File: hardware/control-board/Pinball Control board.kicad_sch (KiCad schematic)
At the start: 108 parts, among them J1 Connector C, J3 B4B-XH-A, J4 Conn_01x10_Pin, J5 Conn_01x10_Pin, Q1 BSS138, Q10 BSS84, Q11 BSS138, Q12 BSS84, Q13 BSS138, Q14 BSS84, Q15 BSS138, Q16 IRFR5410, Q17 IRFR5410, Q18 IRFR5410, Q19 IRFR5410, Q2 BSS138, Q20 IRFR5410, Q3 BSS138, Q4 BSS138, Q5 BSS138, Q6 BSS84, Q7 BSS138, Q8 BSS84, Q9 BSS138, SW1 test switch, SW2 test switch

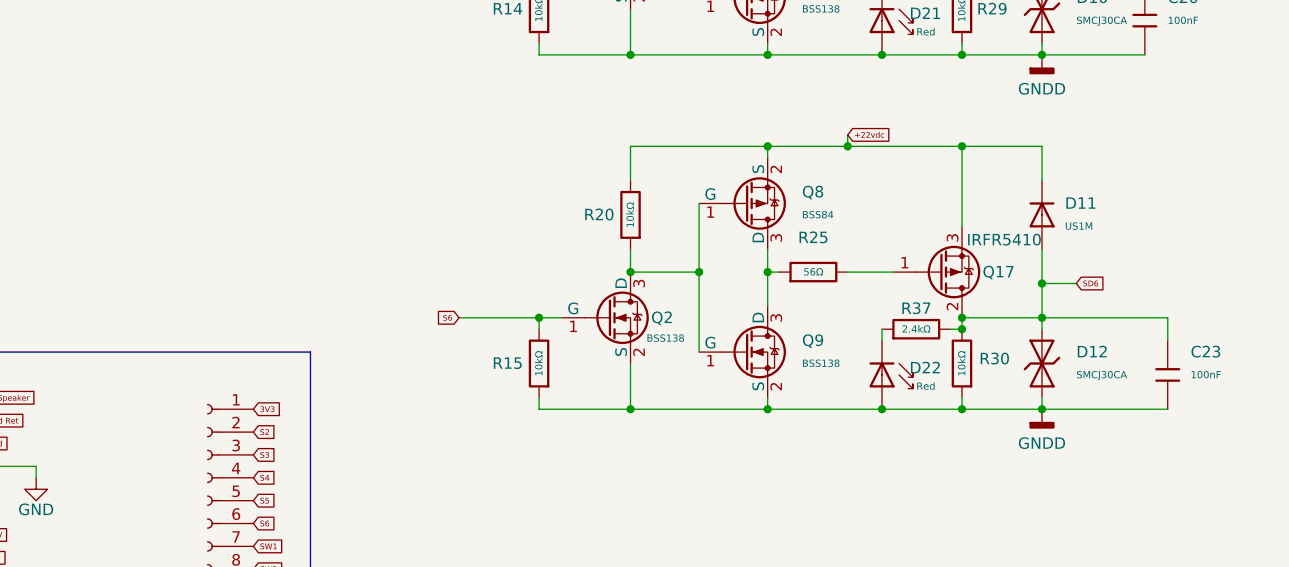
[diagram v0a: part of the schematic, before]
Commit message: Add KiCad note for single-channel solenoid respin
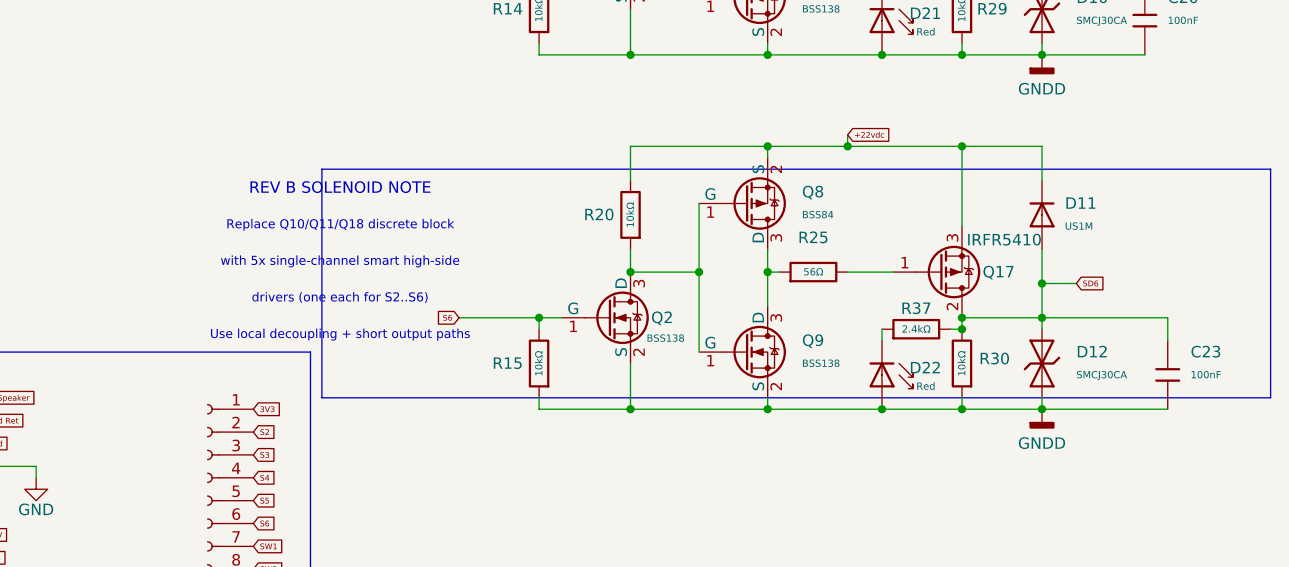
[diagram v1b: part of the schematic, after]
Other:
- note added: "REV B SOLENOID NOTE"
- note added: "Replace Q10/Q11/Q18 discrete block"
- note added: "Use local decoupling + short output paths"
- note added: "drivers (one each for S2..S6)"
- note added: "with 5x single-channel smart high-side"
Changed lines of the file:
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@@
+		)
+	)
+	(rectangle
+		(start 208.28 205.74)
+		(end 313.69 231.14)
+		(stroke
+			(width 0)
+			(type default)
+		)
+		(fill
+			(type none)
+		)
+	)
+	(text "REV B SOLENOID NOTE"
+		(exclude_from_sim no)
+		(at 210.312 208.026 0)
+		(effects
+			(font
+				(size 1.27 1.27)
+			)
+		)
+	)
+	(text "Replace Q10/Q11/Q18 discrete block"
+		(exclude_from_sim no)
+		(at 210.312 212.09 0)
+		(effects
+			(font
+				(size 1 1)
+			)
+		)
+	)
+	(text "with 5x single-channel smart high-side"
+		(exclude_from_sim no)
+		(at 210.312 216.154 0)
+		(effects
+			(font
+				(size 1 1)
+			)
+		)
+	)
+	(text "drivers (one each for S2..S6)"
+		(exclude_from_sim no)
+		(at 210.312 220.218 0)
+		(effects
+			(font
+				(size 1 1)
+			)
+		)
+	)
+	(text "Use local decoupling + short output paths"
+		(exclude_from_sim no)
+		(at 210.312 224.282 0)
+		(effects
+			(font
+				(size 1 1)
+			)
 		)
 	)

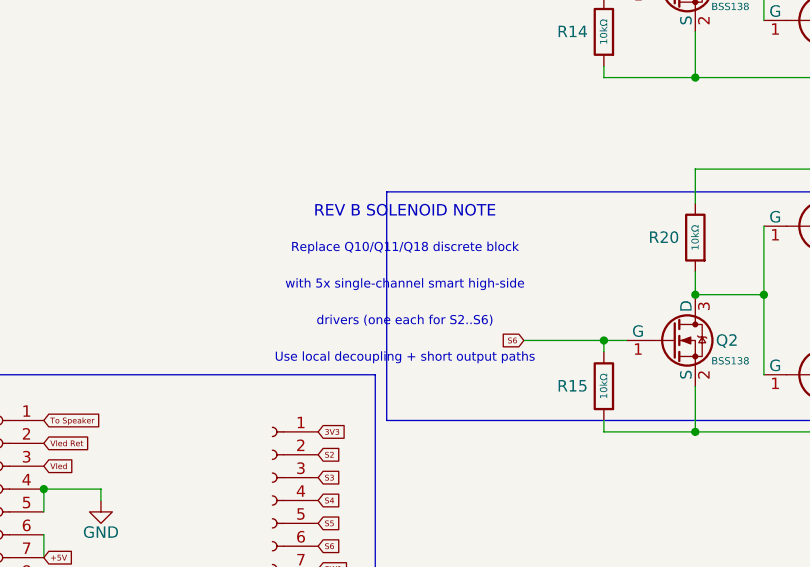
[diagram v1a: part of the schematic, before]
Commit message: Select TPS1H200A-Q1 for solenoid respin
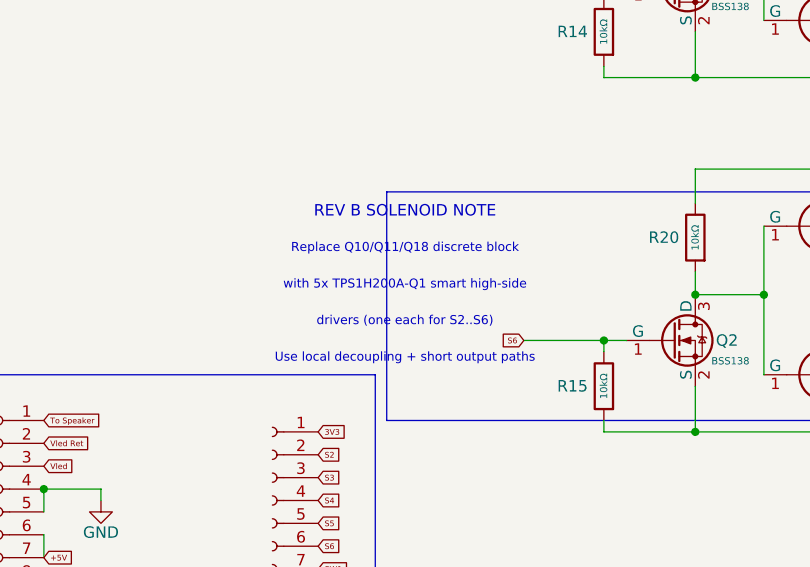
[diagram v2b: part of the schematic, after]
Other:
- note added: "with 5x TPS1H200A-Q1 smart high-side"
- note removed: "with 5x single-channel smart high-side"
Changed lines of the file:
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@@
 		)
 	)
-	(text "with 5x single-channel smart high-side"
+	(text "with 5x TPS1H200A-Q1 smart high-side"
 		(exclude_from_sim no)
 		(at 210.312 216.154 0)

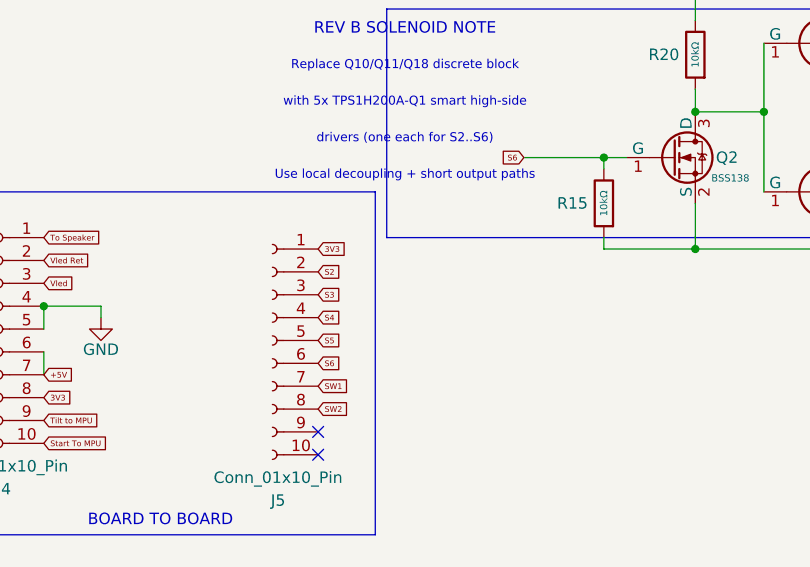
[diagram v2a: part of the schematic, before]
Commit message: Add repo-tracked KiCad library folders and TPS1H200 planning docs
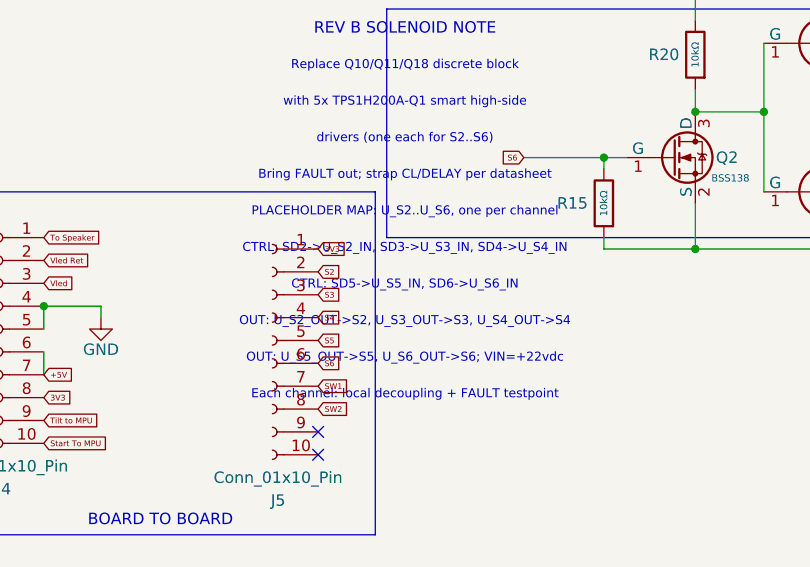
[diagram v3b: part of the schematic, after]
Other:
- note added: "Bring FAULT out; strap CL/DELAY per datasheet"
- note added: "CTRL: SD2->U_S2_IN, SD3->U_S3_IN, SD4->U_S4_IN"
- note added: "CTRL: SD5->U_S5_IN, SD6->U_S6_IN"
- note added: "Each channel: local decoupling + FAULT testpoint"
- note added: "OUT: U_S2_OUT->S2, U_S3_OUT->S3, U_S4_OUT->S4"
- note added: "OUT: U_S5_OUT->S5, U_S6_OUT->S6; VIN=+22vdc"
- note added: "PLACEHOLDER MAP: U_S2..U_S6, one per channel"
- note removed: "Use local decoupling + short output paths"
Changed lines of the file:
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@@
 		)
 	)
-	(text "Use local decoupling + short output paths"
+	(text "Bring FAULT out; strap CL/DELAY per datasheet"
 		(exclude_from_sim no)
 		(at 210.312 224.282 0)
 		(effects
 			(font
+				(size 1 1)
+			)
+		)
+	)
+	(text "PLACEHOLDER MAP: U_S2..U_S6, one per channel"
+		(exclude_from_sim no)
+		(at 210.312 228.346 0)
+		(effects
+			(font
+				(size 1 1)
+			)
+		)
+	)
+	(text "CTRL: SD2->U_S2_IN, SD3->U_S3_IN, SD4->U_S4_IN"
+		(exclude_from_sim no)
+		(at 210.312 232.41 0)
+		(effects
+			(font
+				(size 1 1)
+			)
+		)
+	)
+	(text "CTRL: SD5->U_S5_IN, SD6->U_S6_IN"
+		(exclude_from_sim no)
+		(at 210.312 236.474 0)
+		(effects
+			(font
+				(size 1 1)
+			)
+		)
+	)
+	(text "OUT: U_S2_OUT->S2, U_S3_OUT->S3, U_S4_OUT->S4"
+		(exclude_from_sim no)
+		(at 210.312 240.538 0)
+		(effects
+			(font
+				(size 1 1)
+			)
+		)
+	)
+	(text "OUT: U_S5_OUT->S5, U_S6_OUT->S6; VIN=+22vdc"
+		(exclude_from_sim no)
+		(at 210.312 244.602 0)
+		(effects
+			(font
+				(size 1 1)
+			)
+		)
+	)
+	(text "Each channel: local decoupling + FAULT testpoint"
+		(exclude_from_sim no)
+		(at 210.312 248.666 0)
+		(effects
+			(font

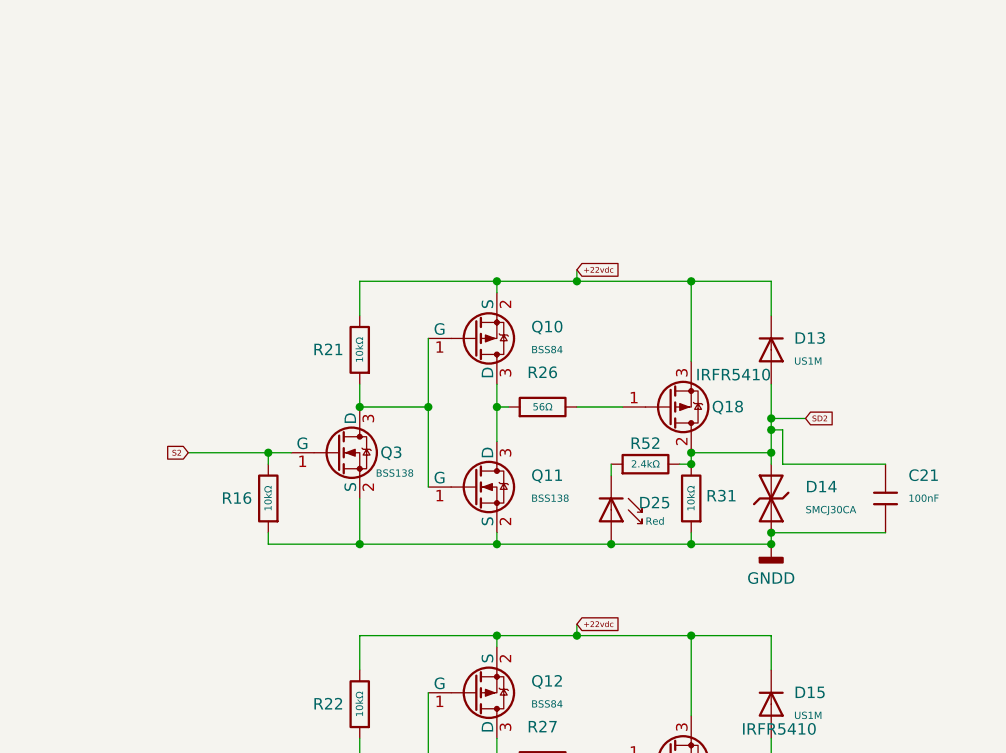
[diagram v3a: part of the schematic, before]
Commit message: Add first TPS1H200 channel prototype to control board schematic
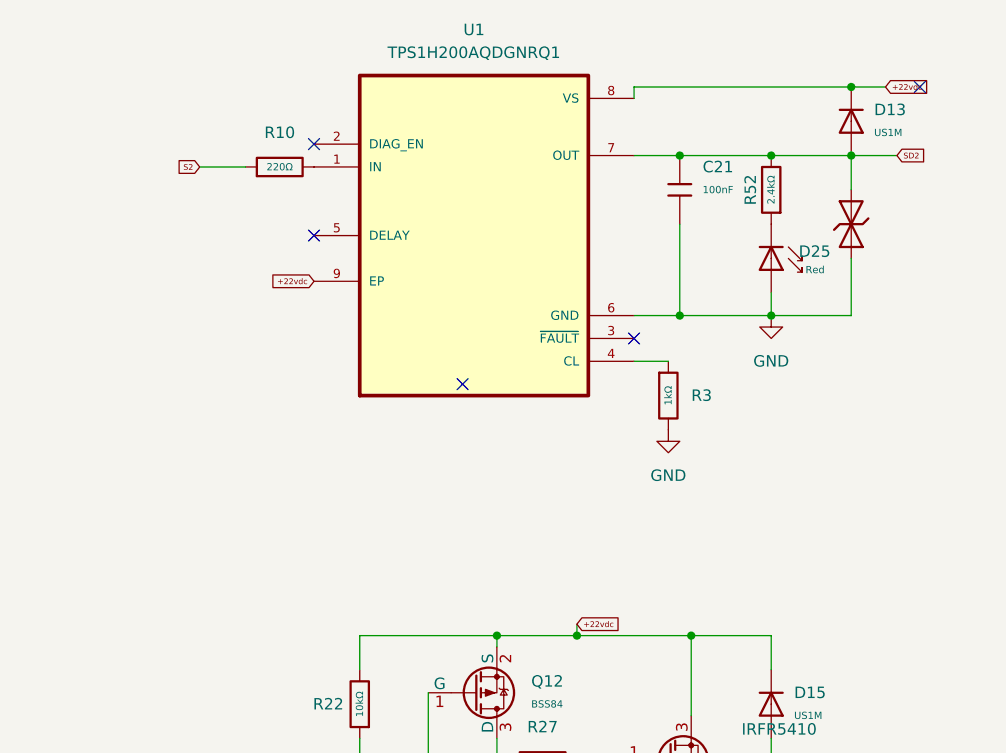
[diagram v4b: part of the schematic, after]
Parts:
- removed Q10: BSS84, PCM_JLCPCB:Q_SOT-23, symbol PCM_JLCPCB-Transistors:PMOS,BSS84
- removed Q11, Q3: BSS138, PCM_JLCPCB:Q_SOT-23, symbol PCM_JLCPCB-Transistors:NMOS,BSS138
- removed Q18: IRFR5410, Package_TO_SOT_SMD:TO-252-2, symbol Transistor_FET:IRF4905
- removed R16, R21, R31: 10kΩ, PCM_JLCPCB:R_0805, symbol PCM_JLCPCB-Resistors:0805,10kΩ
- removed R26: 56Ω, PCM_JLCPCB:R_0805, symbol PCM_JLCPCB-Resistors:0805,56Ω
- added R10: 220Ω, PCM_JLCPCB:R_0805, symbol PCM_JLCPCB-Resistors:0805,220Ω
- added R3: 1kΩ, PCM_JLCPCB:R_0805, symbol PCM_JLCPCB-Resistors:0805,1kΩ
- added U1: TPS1H200AQDGNRQ1, 1My_Parts_ ICs:SOP65P490X110-9N --TSP1H200, symbol 1My_IC's:TPS1H200AQDGNRQ1
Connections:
- net +22vdc: now also U1.8 (VS), U1.9 (EP)
- net GND: now also C21.2, D14.1, D25.2, R3.2, U1.6 (GND)
- net GNDD: no longer C21.2, D14.1, D25.2
- net S2: now also R10.1
- net SD2: now also U1.7 (OUT)
- new net: R3.1, U1.4 (CL)
- new net: R10.2, U1.1 (IN)
- no-connect marks 4 -> 9
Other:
- moved on the sheet: C21, D13, D25, R52

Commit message: Replicate TPS1H200 channels across solenoid outputs
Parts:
- removed C22, C23: 100nF, PCM_JLCPCB:C_0805, symbol PCM_JLCPCB-Capacitors:0805,100nF,(2)
- removed D10, D12, D16: SMCJ30CA, PCM_JLCPCB:D_SMC, symbol PCM_JLCPCB-Diodes:TVS-Bi,SMCJ30CA
- removed D11, D15, D9: US1M, PCM_JLCPCB:D_SMA, symbol PCM_JLCPCB-Diodes:Recovery,US1M
- removed D21, D22, D23, D24: Red, PCM_JLCPCB:D_0805, symbol PCM_JLCPCB-Diodes:LED,0805,Red
- removed Q1, Q13, Q15, Q2, Q4, Q5, Q7, Q9: BSS138, PCM_JLCPCB:Q_SOT-23, symbol PCM_JLCPCB-Transistors:NMOS,BSS138
- removed Q12, Q14, Q6, Q8: BSS84, PCM_JLCPCB:Q_SOT-23, symbol PCM_JLCPCB-Transistors:PMOS,BSS84
- removed Q16, Q17, Q19, Q20: IRFR5410, Package_TO_SOT_SMD:TO-252-2, symbol Transistor_FET:IRF4905
- removed R14, R15, R17, R18, R19, R20, R22, R23, R29, R30, R32, R33: 10kΩ, PCM_JLCPCB:R_0805, symbol PCM_JLCPCB-Resistors:0805,10kΩ
- removed R24, R25, R27, R28: 56Ω, PCM_JLCPCB:R_0805, symbol PCM_JLCPCB-Resistors:0805,56Ω
- removed R34, R37, R50, R51: 2.4kΩ, PCM_JLCPCB:R_0805, symbol PCM_JLCPCB-Resistors:0805,2.4kΩ
- added C17, C18: 100nF, PCM_JLCPCB:C_0805, symbol PCM_JLCPCB-Capacitors:0805,100nF,(2)
- added D11, D12, D13, D14: Red, PCM_JLCPCB:D_0805, symbol PCM_JLCPCB-Diodes:LED,0805,Red
- added D19, D21, D23: US1M, PCM_JLCPCB:D_SMA, symbol PCM_JLCPCB-Diodes:Recovery,US1M
- added D20, D22, D24: SMCJ30CA, PCM_JLCPCB:D_SMC, symbol PCM_JLCPCB-Diodes:TVS-Bi,SMCJ30CA
- added R11, R12, R13, R14: 220Ω, PCM_JLCPCB:R_0805, symbol PCM_JLCPCB-Resistors:0805,220Ω
- added R16, R17, R18, R19: 1kΩ, PCM_JLCPCB:R_0805, symbol PCM_JLCPCB-Resistors:0805,1kΩ
- added R21, R22, R23, R24: 2.4kΩ, PCM_JLCPCB:R_0805, symbol PCM_JLCPCB-Resistors:0805,2.4kΩ
- added U2, U3, U4, U5: TPS1H200AQDGNRQ1, 1My_Parts_ ICs:SOP65P490X110-9N --TSP1H200, symbol 1My_IC's:TPS1H200AQDGNRQ1
- renumbered C2 to C1, C11 to C10, C1 to C11, C13 to C12, C12 to C13, C21 to C16, C3 to C2, C4 to C3, C5 to C4, C6 to C5, C7 to C6, C8 to C7, C9 to C8, C10 to C9, D25 to D10, D13 to D15, D14 to D16, D19 to D9, H4 to H3, H3 to H4, J4 to J2, J5 to J4, R2 to R1, R3 to R15, R9 to R2, R52 to R20, R4 to R3, R5 to R4, R6 to R5, R7 to R6, R1 to R7, R38 to R9
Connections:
- net +22vdc: now also D19.1, D21.1, D23.1, U2.8 (VS), U3.8 (VS), U4.8 (VS), U5.8 (VS); no longer U1.9 (EP)
- net GND: now also C19.2, C20.2, D10.1, D18.1, U1.5 (DELAY), U1.9 (EP), C17.2, C18.2, D11.1, D12.1, D13.1, D14.1, D20.1, D22.1, D24.1, R16.2, R17.2, R18.2, R19.2, U2.5 (DELAY), U2.6 (GND), U2.9 (EP), U3.5 (DELAY), U3.6 (GND), U3.9 (EP), U4.5 (DELAY), U4.6 (GND), U4.9 (EP), U5.5 (DELAY), U5.6 (GND), U5.9 (EP); no longer D10.2
- net GNDD: no longer C19.2, C20.2, D18.1
- net S3: now also R11.1
- net S4: now also R12.1
- net S5: now also R13.1
- net S6: now also R14.1
- net SD3: now also D17.2, D18.2, C17.1, R21.2, U2.7 (OUT); no longer C19.1
- net SD4: now also C18.1, D19.2, D20.2, R22.2, U3.7 (OUT); no longer D17.2, D18.2
- net SD5: now also C19.1, D21.2, D22.2, R23.2, U4.7 (OUT); no longer C20.1
- net SD6: now also C20.1, D23.2, D24.2, R24.2, U5.7 (OUT)
- net at R20.1: now also D10.2; no longer D10.1
- new net: R17.1, U3.4 (CL)
- new net: R11.2, U2.1 (IN)
- new net: R16.1, U2.4 (CL)
- new net: R14.2, U5.1 (IN)
- new net: R19.1, U5.4 (CL)
- new net: R12.2, U3.1 (IN)
- new net: D12.2, R22.1
- new net: R13.2, U4.1 (IN)
- new net: R18.1, U4.4 (CL)
- new net: D13.2, R23.1
- new net: D14.2, R24.1
- new net: D11.2, R21.1
- no-connect marks 9 -> 14
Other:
- moved on the sheet: D10, J2, J4

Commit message: Align TPS1H200 footprints to project library
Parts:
- U1, U2, U3, U4, U5: footprint 1My_Parts_ ICs:SOP65P490X110-9N --TSP1H200 -> Snapmagic_TI_TPS1H200A_Q1:SOP65P490X110-9N
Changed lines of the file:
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@@
 			)
 		)
-		(property "Footprint" "1My_Parts_ ICs:SOP65P490X110-9N --TSP1H200"
+		(property "Footprint" "Snapmagic_TI_TPS1H200A_Q1:SOP65P490X110-9N"
 			(at 256.54 88.9 0)
 			(effects
@@
 			)
 		)
-		(property "Footprint" "1My_Parts_ ICs:SOP65P490X110-9N --TSP1H200"
+		(property "Footprint" "Snapmagic_TI_TPS1H200A_Q1:SOP65P490X110-9N"
 			(at 257.81 241.3 0)
 			(effects
@@
 			)
 		)
-		(property "Footprint" "1My_Parts_ ICs:SOP65P490X110-9N --TSP1H200"
+		(property "Footprint" "Snapmagic_TI_TPS1H200A_Q1:SOP65P490X110-9N"
 			(at 256.54 190.5 0)
 			(effects
@@
 			)
 		)
-		(property "Footprint" "1My_Parts_ ICs:SOP65P490X110-9N --TSP1H200"
+		(property "Footprint" "Snapmagic_TI_TPS1H200A_Q1:SOP65P490X110-9N"
 			(at 256.54 139.7 0)
 			(effects
@@
 			)
 		)
-		(property "Footprint" "1My_Parts_ ICs:SOP65P490X110-9N --TSP1H200"
+		(property "Footprint" "Snapmagic_TI_TPS1H200A_Q1:SOP65P490X110-9N"
 			(at 256.54 39.37 0)
 			(effects
